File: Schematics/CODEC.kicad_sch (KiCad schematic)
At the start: 9 parts, among them U1 PCM3060

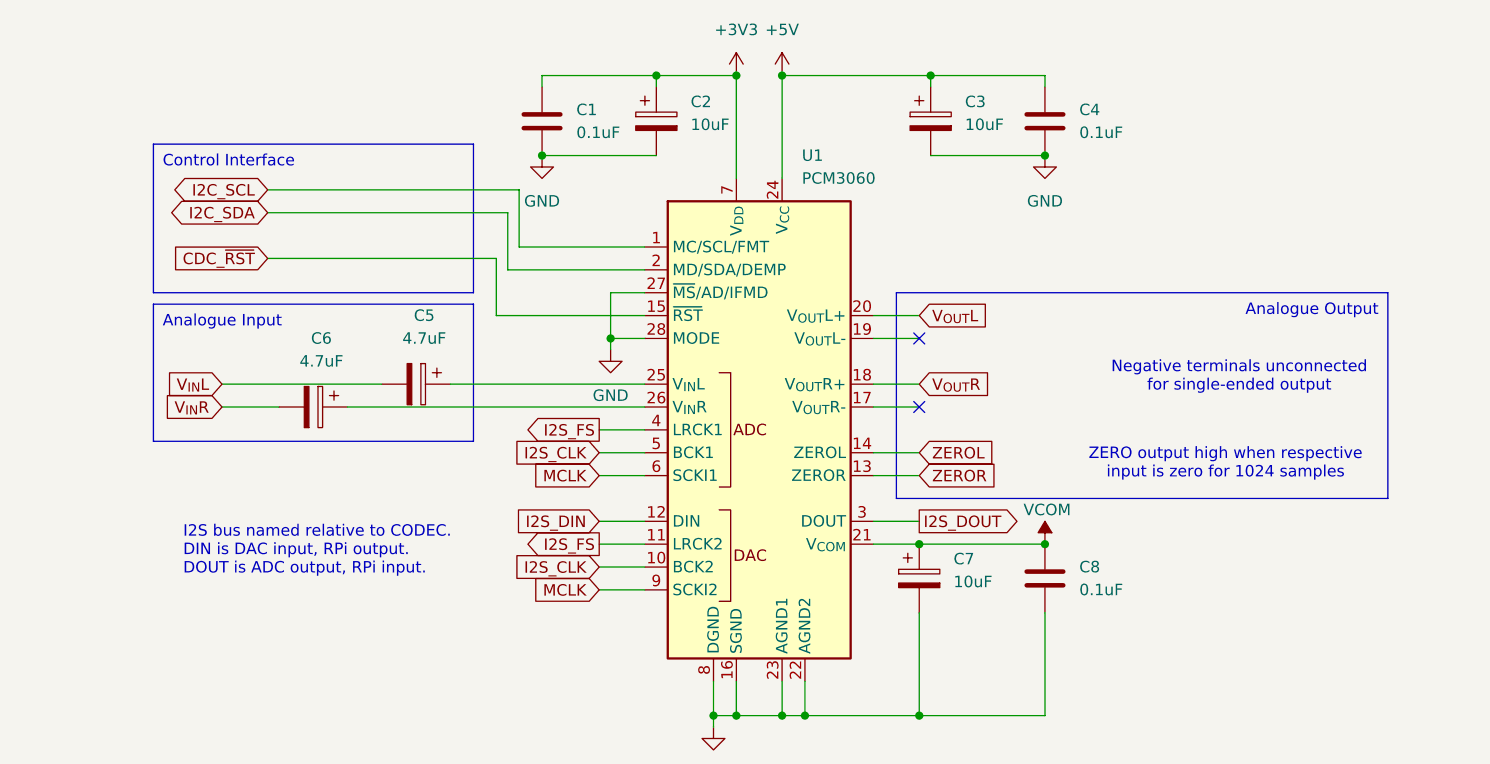
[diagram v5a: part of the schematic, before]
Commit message: Updated to KiCAD v9
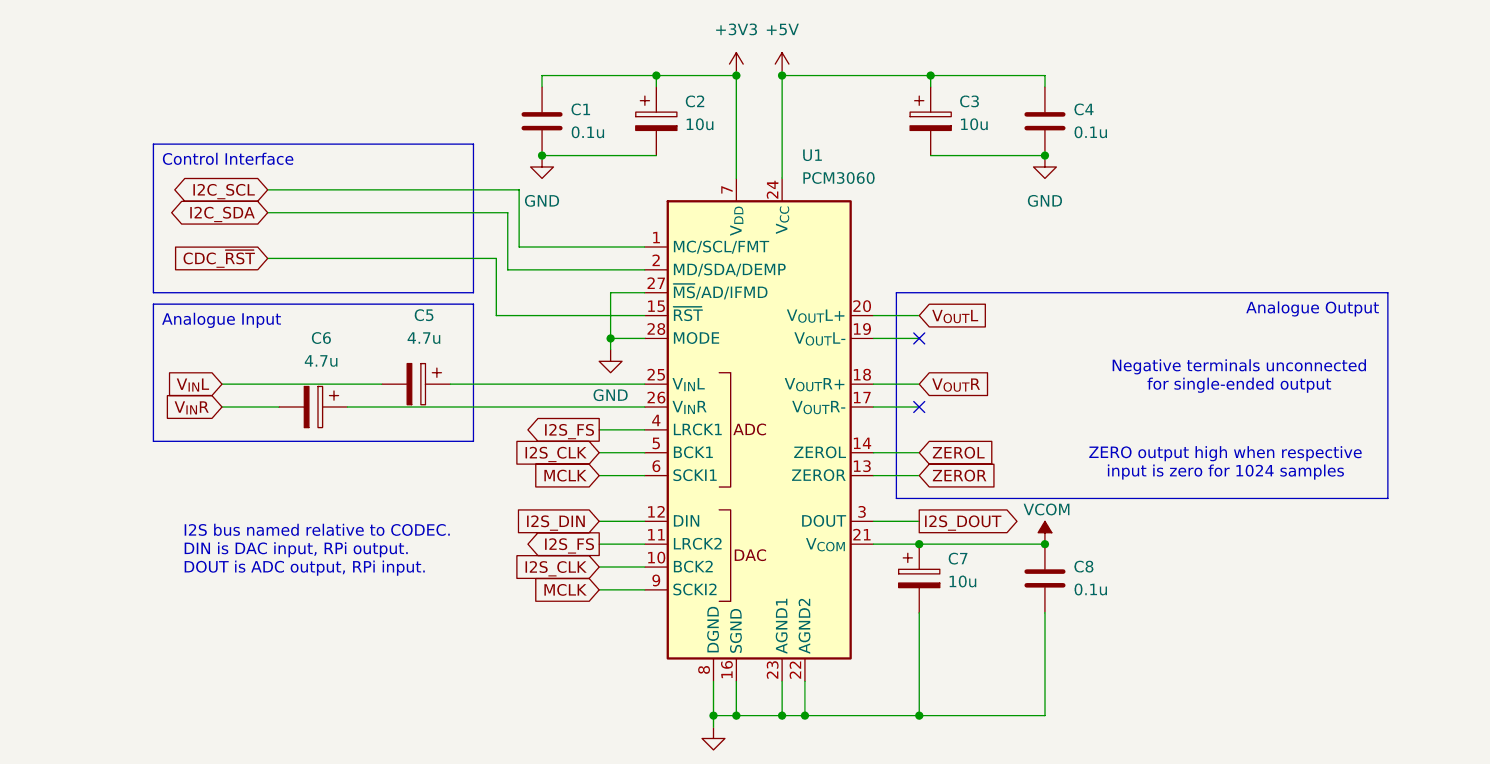
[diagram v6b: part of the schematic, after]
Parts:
- C1, C4, C8: value 0.1uF -> 0.1u
- C2, C3, C7: value 10uF -> 10u; footprint (none) -> Capacitor_SMD:CP_Elec_5x5.4
- C5, C6: value 4.7uF -> 4.7u
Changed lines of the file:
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@@
 (kicad_sch
-	(version 20231120)
+	(version 20250114)
 	(generator "eeschema")
-	(generator_version "8.0")
+	(generator_version "9.0")
 	(paper "A4")
 	(title_block
@@
 		(date "2025-02-12")
 	)
+	(text "Slave Address:\n0b100011(ADR)(R/~{W})\n\nMODE Operation:\nSPI Mode: Direct to VDD.\nI2C Mode: Direct to DGND.\nSingle-Ended HW Mode: 220k pull-up to VDD.\nDifferential HW Mode: 220k pull-down to DGND.\n\nClocks:\nLRCK (FS): Audio data left/right clock, left is low, right is high.\nBCK (SCK): Audio data bit clock (48 or 64 times sample rate).\nSCKI (MCLK): System clock input (2.048-36.864MHz, 128, 192, 256, 384, 512, or 768 times sample rate)."
+		(exclude_from_sim no)
+		(at 13.208 172.974 0)
+		(effects
+			(font
+				(size 1.27 1.27)
+			)
+			(justify left)
+		)
+	)
+	(text "Negative terminals unconnected \nfor single-ended output"
+		(exclude_from_sim no)
+		(at 197.485 88.138 0)
+		(effects
+			(font
+				(size 1.27 1.27)
+			)
+		)
+	)
+	(text "Drawn by Harvey McBurney"
+		(exclude_from_sim no)
+		(at 198.882 169.672 0)
+		(effects
+			(font
+				(size 2 2)
+				(thickness 0.6)
+				(bold yes)
+			)
+		)
+	)
+	(text "ZERO output high when respective \ninput is zero for 1024 samples"
+		(exclude_from_sim no)
+		(at 195.961 97.79 0)
+		(effects
+			(font
+				(size 1.27 1.27)
+			)
+		)
+	)
+	(text "I2S bus named relative to CODEC.\nDIN is DAC input, RPi output.\nDOUT is ADC output, RPi input."
+		(exclude_from_sim no)
+		(at 80.137 107.442 0)
+		(effects
+			(font
+				(size 1.27 1.27)
+			)
+			(justify left)
+		)
+	)
+	(text_box "Control Interface"
+		(exclude_from_sim no)
+		(at 76.835 62.23 0)
+		(size 35.56 16.51)
+		(margins 0.9525 0.9525 0.9525 0.9525)
+		(stroke
+			(width 0)
+			(type default)
+		)
+		(fill
+			(type none)
+		)
+		(effects
+			(font
+				(size 1.27 1.27)
+			)
+			(justify left top)
+		)
+	)
+	(text_box "Analogue Output"
+		(exclude_from_sim no)
+		(at 159.385 78.74 0)
+		(size 54.61 22.86)
+		(margins 0.9525 0.9525 0.9525 0.9525)
+		(stroke
+			(width 0)
+			(type default)
+		)
+		(fill
+			(type none)
+		)
+		(effects
+			(font
+				(size 1.27 1.27)
+			)
+			(justify right top)
+		)
+	)
+	(text_box "Analogue Input"
+		(exclude_from_sim no)
+		(at 76.835 80.01 0)
+		(size 35.56 15.24)
+		(margins 0.9525 0.9525 0.9525 0.9525)
+		(stroke
+			(width 0)
+			(type default)
+		)
+		(fill
+			(type none)
+		)
+		(effects
+			(font
+				(size 1.27 1.27)
+			)
+			(justify left top)
+		)
+	)
 	(junction
 		(at 146.685 54.61)
@@
 		)
 	)
-	(text_box "Control Interface"
-		(exclude_from_sim no)
-		(at 76.835 62.23 0)
-		(size 35.56 16.51)
-		(stroke
-			(width 0)
-			(type default)
-		)
-		(fill
-			(type none)
-		)
-		(effects
-			(font
-				(size 1.27 1.27)
-			)
-			(justify left top)
-		)
-	)
-	(text_box "Analogue Output"
-		(exclude_from_sim no)
-		(at 159.385 78.74 0)
-		(size 54.61 22.86)
-		(stroke
-			(width 0)
-			(type default)
-		)
-		(fill
-			(type none)
-		)
-		(effects
-			(font
-				(size 1.27 1.27)
-			)
-			(justify right top)
-		)
-	)
-	(text_box "Analogue Input"
-		(exclude_from_sim no)
-		(at 76.835 80.01 0)
-		(size 35.56 15.24)
-		(stroke
-			(width 0)
-			(type default)
-		)
-		(fill
-			(type none)
-		)
-		(effects
-			(font
-				(size 1.27 1.27)
-			)
-			(justify left top)
-		)
-	)
-	(text "Slave Address:\n0b100011(ADR)(R/~{W})\n\nMODE Operation:\nSPI Mode: Direct to VDD.\nI2C Mode: Direct to DGND.\nSingle-Ended HW Mode: 220k pull-up to VDD.\nDifferential HW Mode: 220k pull-down to DGND.\n\nClocks:\nLRCK (FS): Audio data left/right clock, left is low, right is high.\nBCK (SCK): Audio data bit clock (48 or 64 times sample rate).\nSCKI (MCLK): System clock input (2.048-36.864MHz, 128, 192, 256, 384, 512, or 768 times sample rate)."
-		(exclude_from_sim no)
-		(at 13.208 172.974 0)
-		(effects
-			(font
-				(size 1.27 1.27)
-			)
-			(justify left)
-		)
-	)
-	(text "Negative terminals unconnected \nfor single-ended output"
-		(exclude_from_sim no)
-		(at 197.485 88.138 0)
-		(effects
-			(font
-				(size 1.27 1.27)
-			)
-		)
-	)
-	(text "Drawn by Harvey McBurney"
-		(exclude_from_sim no)
-		(at 198.882 169.672 0)
-		(effects
-			(font
-				(size 2 2)
-				(thickness 0.6)
-				(bold yes)
-			)
-		)
-	)
-	(text "ZERO output high when respective \ninput is zero for 1024 samples"
-		(exclude_from_sim no)
-		(at 195.961 97.79 0)
-		(effects
-			(font
-				(size 1.27 1.27)
-			)
-		)
-	)
-	(text "I2S bus named relative to CODEC.\nDIN is DAC input, RPi output.\nDOUT is ADC output, RPi input."
-		(exclude_from_sim no)
-		(at 80.137 107.442 0)
-		(effects
-			(font
-				(size 1.27 1.27)
-			)
-			(justify left)
-		)
-	)
 	(global_label "V_{OUT}L"
 		(shape input)
@@
 		(fields_autoplaced yes)
 		(property "Reference" "C1"
-			(at 123.825 58.4199 0)
+			(at 123.19 58.4199 0)
 			(effects
 				(font
@@
 			)
 		)
-		(property "Value" "0.1uF"
-			(at 123.825 60.9599 0)
+		(property "Value" "0.1u"
+			(at 123.19 60.9599 0)
 			(effects
 				(font
@@
 		(fields_autoplaced yes)
 		(property "Reference" "C7"
-			(at 165.735 108.3309 0)
+			(at 165.1 108.3309 0)
 			(effects
 				(font
@@
 			)
 		)
-		(property "Value" "10uF"
-			(at 165.735 110.8709 0)
+		(property "Value" "10u"
+			(at 165.1 110.8709 0)
 			(effects
 				(font
@@
 			)
 		)
-		(property "Footprint" ""
+		(property "Footprint" "Capacitor_SMD:CP_Elec_5x5.4"
 			(at 162.8902 114.3 0)
 			(effects
@@
 		(fields_autoplaced yes)
 		(property "Reference" "C4"
-			(at 179.705 58.4199 0)
+			(at 179.07 58.4199 0)
 			(effects
 				(font
@@
 			)
 		)
-		(property "Value" "0.1uF"
-			(at 179.705 60.9599 0)
+		(property "Value" "0.1u"
+			(at 179.07 60.9599 0)
 			(effects
 				(font
@@
 			)
 		)
-		(property "Value" "4.7uF"
+		(property "Value" "4.7u"
 			(at 95.504 86.36 90)
 			(effects
@@
 		(fields_autoplaced yes)
 		(property "Reference" "C8"
-			(at 179.705 109.2199 0)
+			(at 179.07 109.2199 0)
 			(effects
 				(font
@@
 			)
 		)
-		(property "Value" "0.1uF"
-			(at 179.705 111.7599 0)
+		(property "Value" "0.1u"
+			(at 179.07 111.7599 0)
 			(effects
 				(font
@@
 		(fields_autoplaced yes)
 		(property "Reference" "C2"
-			(at 136.525 57.5309 0)
+			(at 135.89 57.5309 0)
 			(effects
 				(font
@@
 			)
 		)
-		(property "Value" "10uF"
-			(at 136.525 60.0709 0)
+		(property "Value" "10u"
+			(at 135.89 60.0709 0)
 			(effects
 				(font
@@
 			)
 		)
-		(property "Footprint" ""
+		(property "Footprint" "Capacitor_SMD:CP_Elec_5x5.4"
 			(at 133.6802 63.5 0)
 			(effects
@@
 			)
 		)
-		(property "Value" "4.7uF"
+		(property "Value" "4.7u"
 			(at 106.934 83.82 90)
 			(effects
@@
 		(fields_autoplaced yes)
 		(property "Reference" "C3"
-			(at 167.005 57.5309 0)
+			(at 166.37 57.5309 0)
 			(effects
 				(font
@@
 			)
 		)
-		(property "Value" "10uF"
-			(at 167.005 60.0709 0)
+		(property "Value" "10u"
+			(at 166.37 60.0709 0)
 			(effects
 				(font
@@
 			)
 		)
-		(property "Footprint" ""
+		(property "Footprint" "Capacitor_SMD:CP_Elec_5x5.4"
 			(at 164.1602 63.5 0)
 			(effects

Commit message: Added all footprints, updated PCB
Added footprints using uni available components where possible. Might be necessary to change op-amps as they are large and not made for audio. PCB has a mockup of component placements but probably needs expanded.
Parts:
- C1, C4, C8: footprint (none) -> Capacitor_SMD:C_0805_2012Metric_Pad1.18x1.45mm_HandSolder
- C5, C6: footprint (none) -> Capacitor_SMD:CP_Elec_4x5.7
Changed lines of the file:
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@@
 			)
 		)
-		(property "Footprint" ""
+		(property "Footprint" "Capacitor_SMD:C_0805_2012Metric_Pad1.18x1.45mm_HandSolder"
 			(at 120.9802 63.5 0)
 			(effects
@@
 			)
 		)
-		(property "Footprint" ""
+		(property "Footprint" "Capacitor_SMD:C_0805_2012Metric_Pad1.18x1.45mm_HandSolder"
 			(at 176.8602 63.5 0)
 			(effects
@@
 			)
 		)
-		(property "Footprint" ""
+		(property "Footprint" "Capacitor_SMD:CP_Elec_4x5.7"
 			(at 90.805 92.4052 0)
 			(effects
@@
 			)
 		)
-		(property "Footprint" ""
+		(property "Footprint" "Capacitor_SMD:C_0805_2012Metric_Pad1.18x1.45mm_HandSolder"
 			(at 176.8602 114.3 0)
 			(effects
@@
 			)
 		)
-		(property "Footprint" ""
+		(property "Footprint" "Capacitor_SMD:CP_Elec_4x5.7"
 			(at 102.235 89.8652 0)
 			(effects

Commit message: Adjusted Capacitor Footprints
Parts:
- C2, C3, C7: footprint Capacitor_SMD:CP_Elec_5x5.4 -> Capacitor_SMD:CP_Elec_4x5.7
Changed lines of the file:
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@@
 			)
 		)
-		(property "Footprint" "Capacitor_SMD:CP_Elec_5x5.4"
+		(property "Footprint" "Capacitor_SMD:CP_Elec_4x5.7"
 			(at 162.8902 114.3 0)
 			(effects
@@
 			)
 		)
-		(property "Footprint" "Capacitor_SMD:CP_Elec_5x5.4"
+		(property "Footprint" "Capacitor_SMD:CP_Elec_4x5.7"
 			(at 133.6802 63.5 0)
 			(effects
@@
 			)
 		)
-		(property "Footprint" "Capacitor_SMD:CP_Elec_5x5.4"
+		(property "Footprint" "Capacitor_SMD:CP_Elec_4x5.7"
 			(at 164.1602 63.5 0)
 			(effects
